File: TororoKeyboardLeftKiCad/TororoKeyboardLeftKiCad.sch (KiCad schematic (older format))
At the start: 90 parts, among them J1 MJ-4PP-9, SW1 SW_PUSH, SW10 SW_PUSH, SW11 SW_PUSH, SW12 SW_PUSH, SW13 SW_PUSH, SW14 SW_PUSH, SW15 SW_PUSH, SW16 SW_PUSH, SW17 SW_PUSH, SW18 SW_PUSH, SW19 SW_PUSH, SW2 SW_PUSH, SW20 SW_PUSH, SW21 SW_PUSH, SW22 SW_PUSH, SW23 SW_PUSH, SW24 SW_PUSH, SW25 SW_PUSH, SW26 SW_PUSH, SW27 SW_PUSH, SW28 SW_PUSH, SW29 SW_PUSH, SW3 SW_PUSH, SW4 SW_PUSH, SW5 SW_PUSH, SW6 SW_PUSH, SW7 SW_PUSH, SW8 SW_PUSH, SW9 SW_PUSH, U1 ProMicro

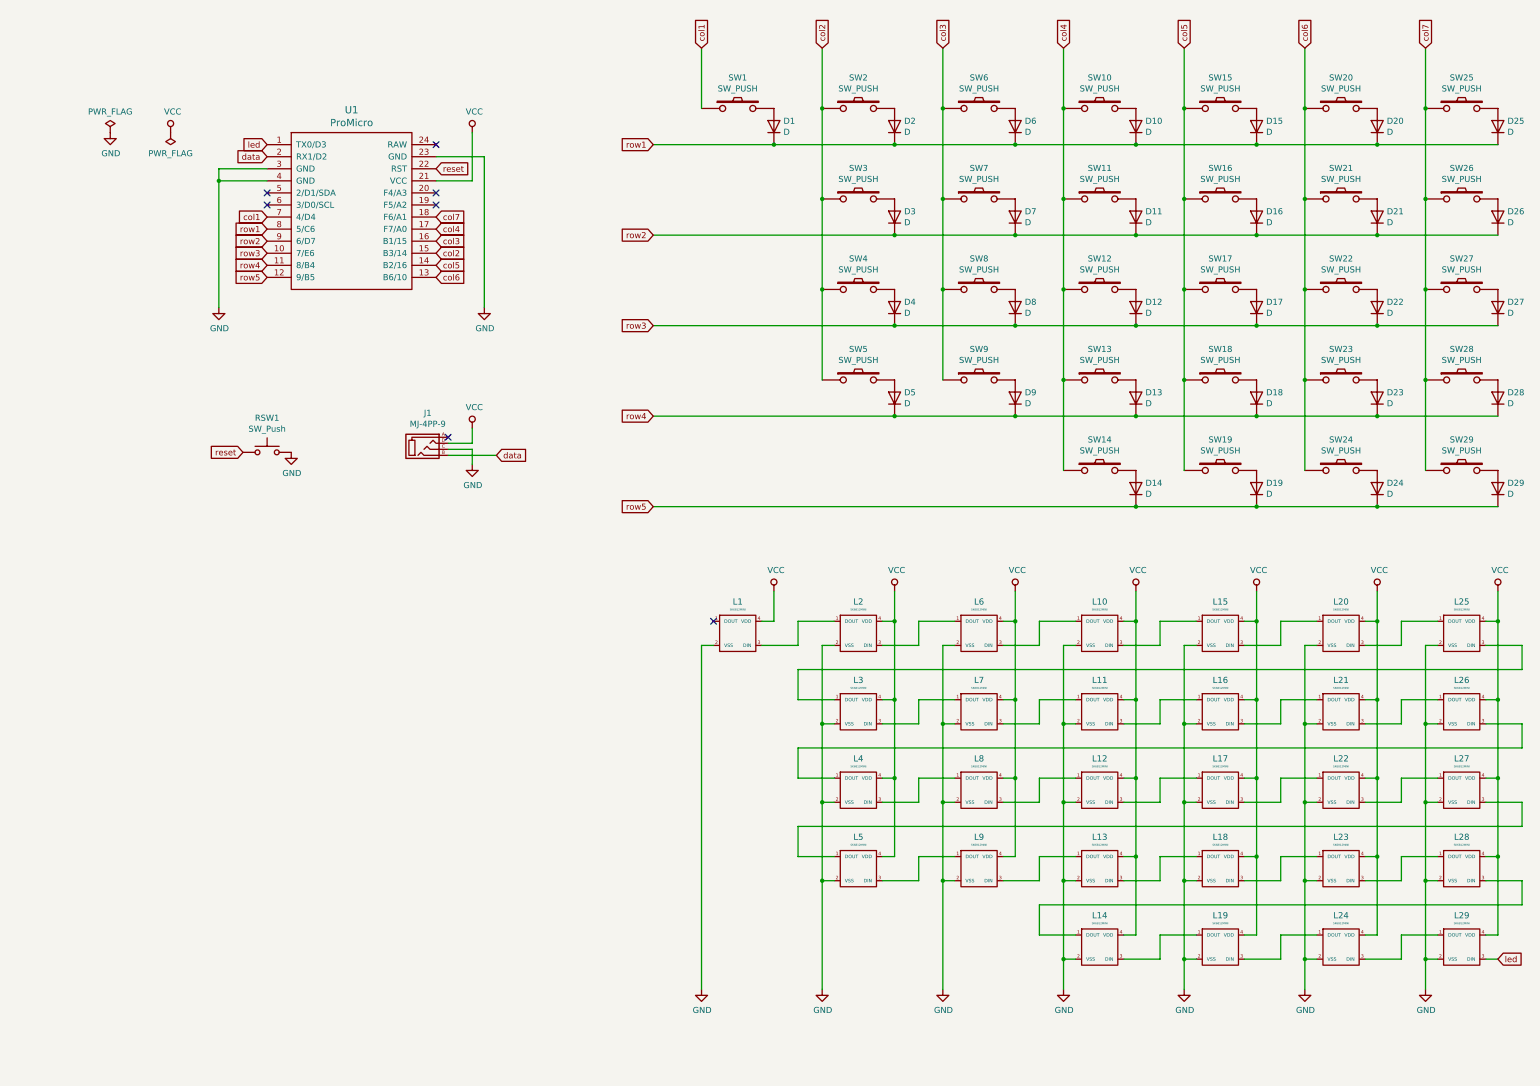
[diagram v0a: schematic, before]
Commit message: 左手側の回路図を整理しネットリストを追加
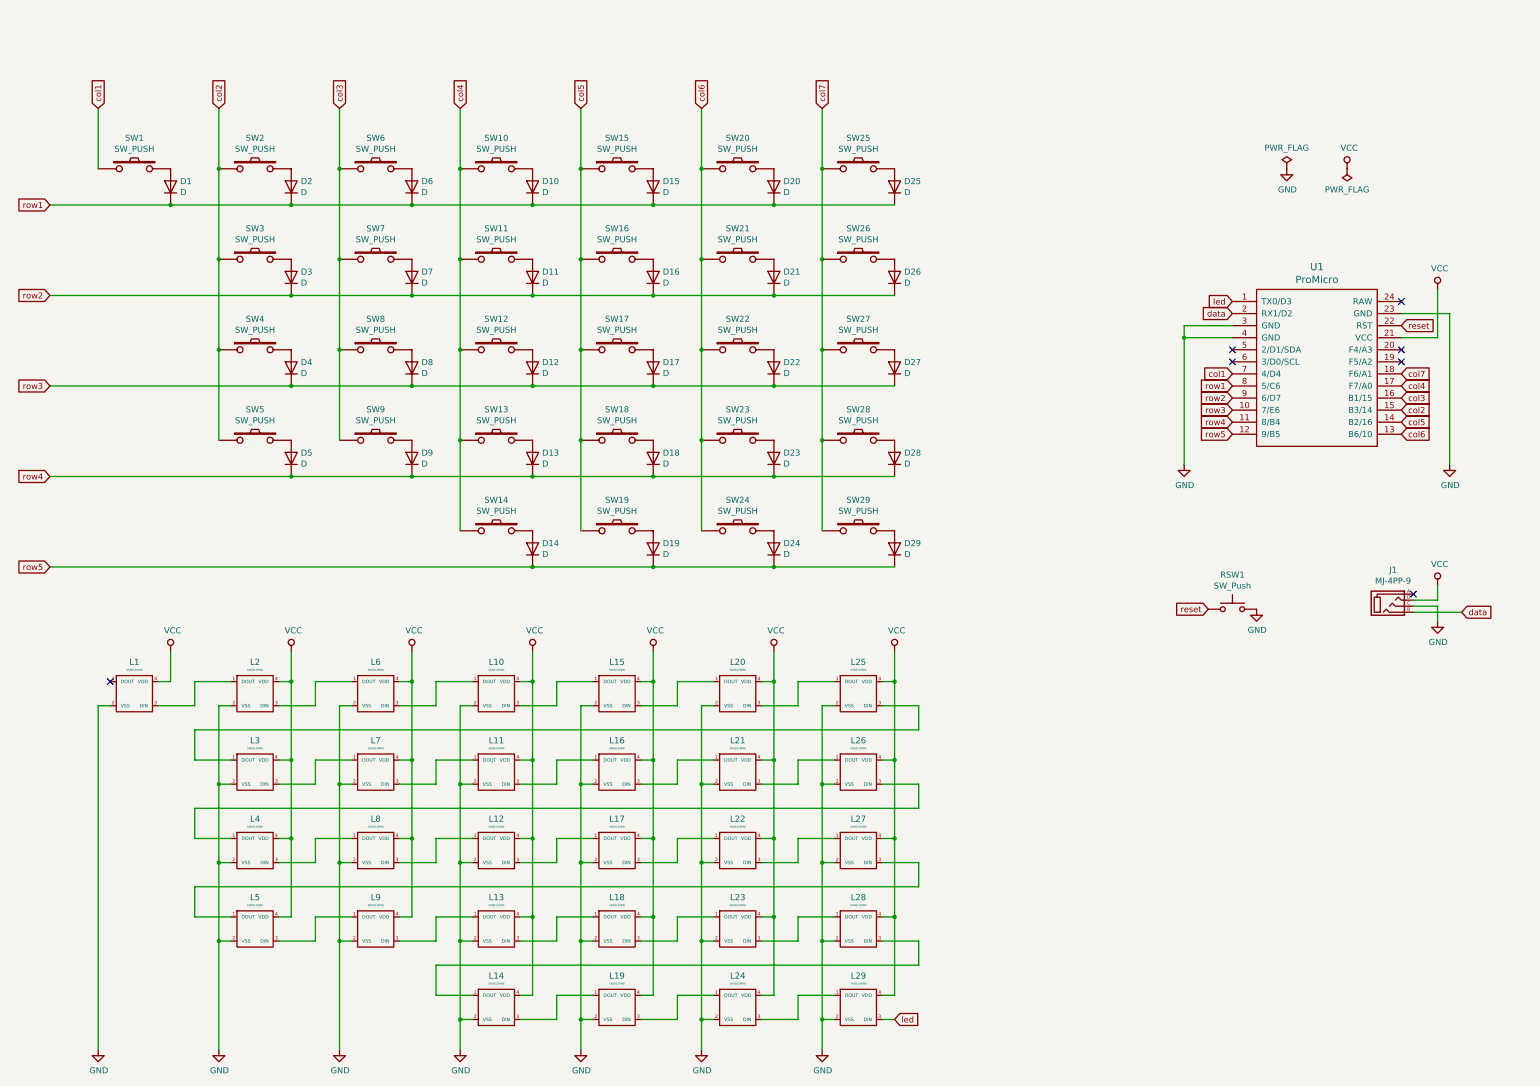
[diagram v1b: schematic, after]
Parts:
- D1, D10, D11, D12, D13, D14, D15, D16, D17, D18, D19, D2, D20, D21, D22, D23, D24, D25, D26, D27, D28, D29, D3, D4, D5, D6, D7, D8, D9: footprint (none) -> kbd_tororo:D3_TH_SMD_top
- J1: footprint (none) -> kbd_tororo:MJ-4PP-9_back
- L1, L10, L11, L12, L13, L14, L15, L16, L17, L18, L19, L2, L20, L21, L22, L23, L24, L25, L26, L27, L28, L29, L3, L4, L5, L6, L7, L8, L9: footprint (none) -> kbd_tororo:SK6812MINI_back
- RSW1: footprint (none) -> kbd_tororo:ResetSW_back
- SW1, SW10, SW11, SW12, SW13, SW14, SW15, SW16, SW17, SW18, SW19, SW2, SW20, SW21, SW22, SW23, SW24, SW25, SW26, SW27, SW28, SW29, SW3, SW4, SW5, SW6, SW7, SW8, SW9: footprint (none) -> kbd_tororo:Hybrid_PCB_100H_no-silk_no_ref
- U1: footprint (none) -> kbd_tororo:ProMicro_v2_back
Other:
- moved on the sheet: D1, D10, D11, D12, D13, D14, D15, D16, D17, D18, D19, D2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
